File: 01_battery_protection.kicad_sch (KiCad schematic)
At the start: 20 parts, among them J1 JST B5B-XH-A, J2 Molex 43045-0200, Q1 CSD18540Q5B, Q2 CSD18540Q5B, Q3 AO3401A, U1 BQ76920PW

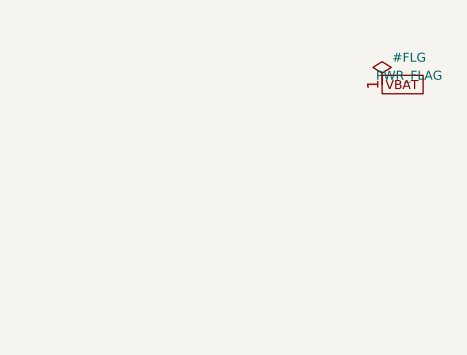
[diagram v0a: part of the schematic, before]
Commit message: Sheet 2: USB-C Charging Input (TPS25751 PD controller + BQ25792 buck-boost charger)
Merged all 5 hand-built project-local symbols into libs/red-light-panel.kicad_sym
(matching the single project-local sym-lib-table entry). Fixed duplicate-pad
pins on BQ25792 (BAT) and TPS25751 (VBUS) from power_out to passive -- ERC
correctly flagged two power_out pins tied together as a conflict even
though they're the same physical lead on the IC.

0 ERC errors except the two expected cross-sheet dependencies (I2Ct_SCL
driven by the MCU on sheet 6; VIN_3V3 driven by sheet 3's buck regulator).
See tools/kicad_gen/sheet2.py docstring for the substantial list of
flagged topology judgment calls (TPS25751 power-path pin ambiguity, BQ25792
front-end ideal-diode MOSFETs not in original BOM, added inductor/set
resistors, etc).

Co-Authored-By: Claude Sonnet 5 <noreply@anthropic.com>
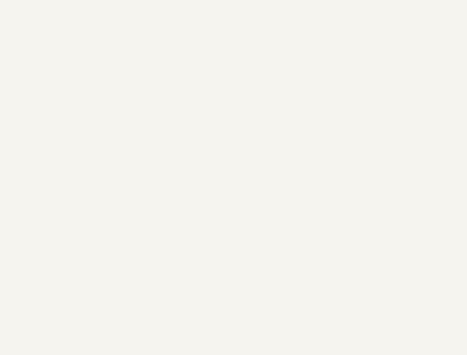
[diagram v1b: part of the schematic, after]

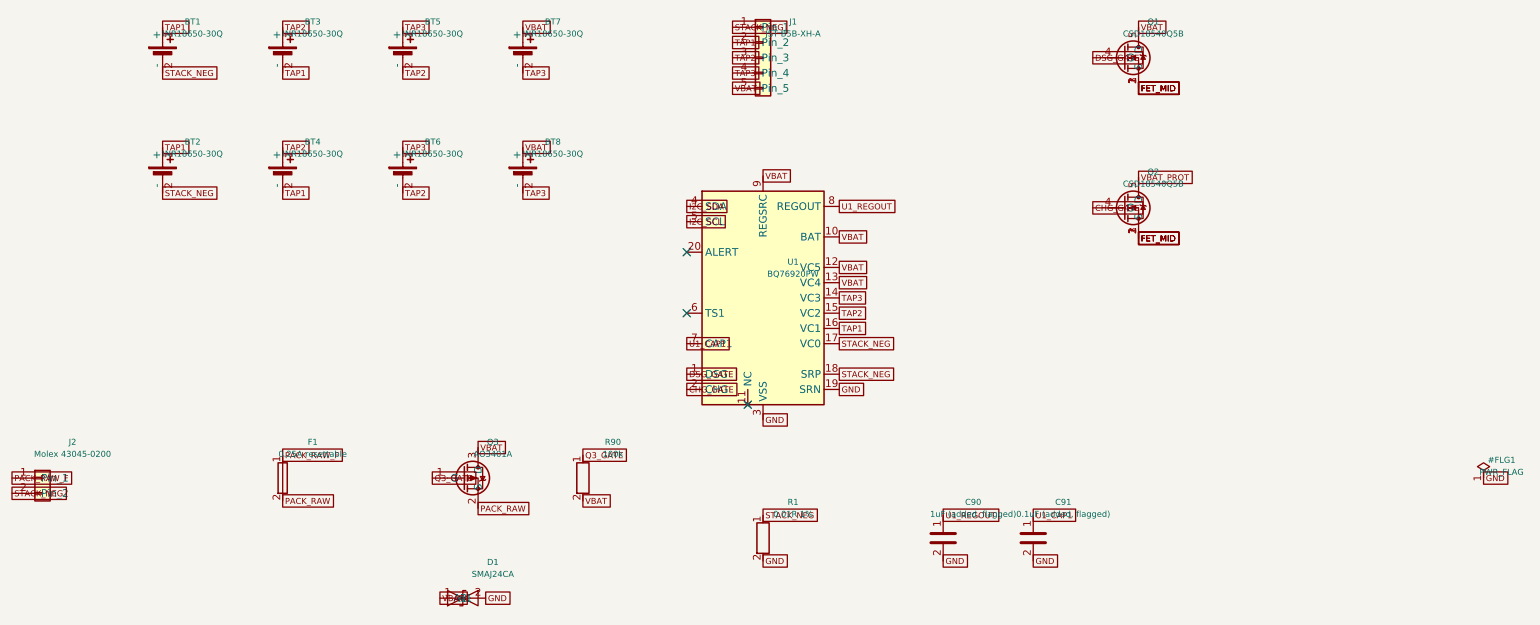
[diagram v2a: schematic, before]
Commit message: Schematic: replace global-label power nets with real power symbols
GND, VBAT, VBAT_PROT, 3V3, and USB_VBUS now get an actual KiCad power
symbol at every pin (power:GND, power:+3V3 with Value overridden to
'3V3', power:VBUS overridden to 'USB_VBUS', and two custom symbols for
VBAT/VBAT_PROT copied from stock power:+BATT into
libs/red-light-panel.kicad_sym) instead of a plain GlobalLabel -- the
idiomatic convention for power rails. All other cross-sheet signal nets
(I2C, PWM, LED channel outputs, etc.) remain GlobalLabels, which still
makes sense for data/PWM signals.

Confirmed empirically before rolling this out: overriding a stock power
symbol's Value does change its effective net name (power:+3V3 with
Value='3V3' correctly nets as '3V3'), and every power symbol's pin is
still power_in (never power_out), so existing PWR_FLAG placements are
unaffected. 0 ERC errors after the change; BOM still 153 components /
48 grouped rows, zero blank footprints, zero duplicate references.

Co-Authored-By: Claude Sonnet 5 <noreply@anthropic.com>
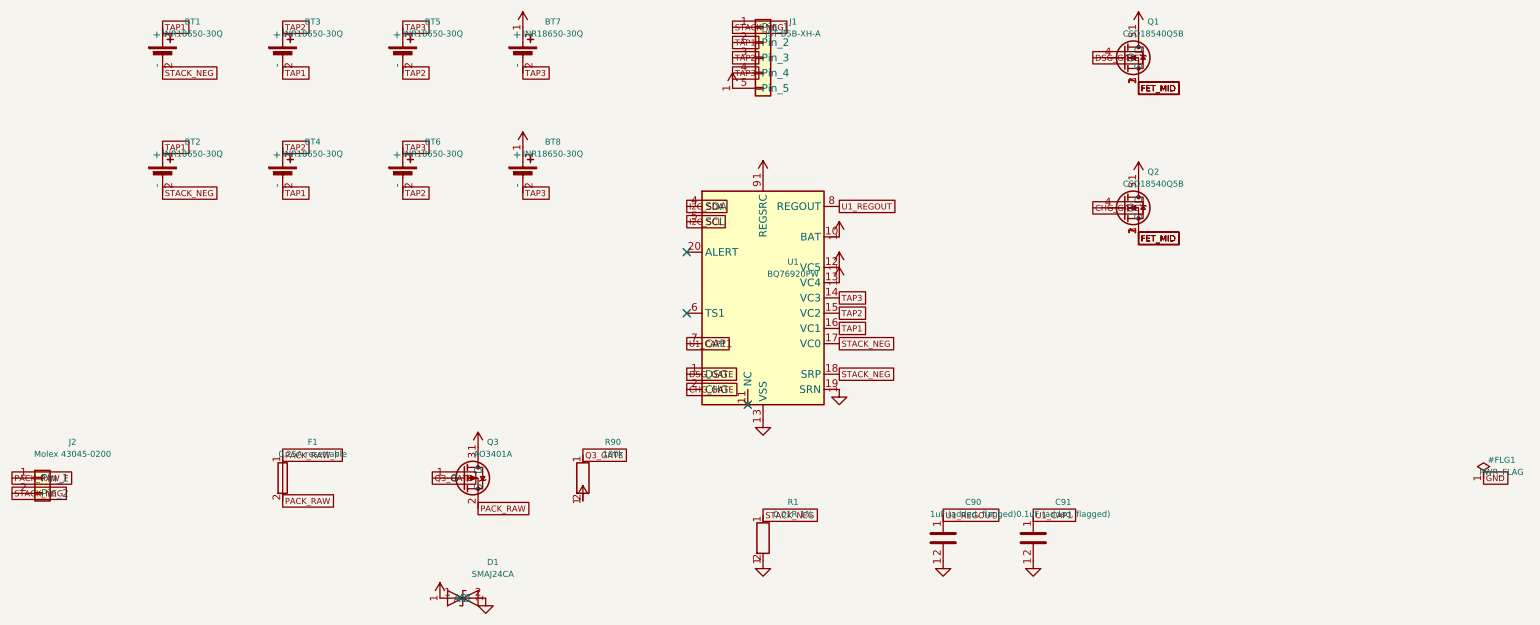
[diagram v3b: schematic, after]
